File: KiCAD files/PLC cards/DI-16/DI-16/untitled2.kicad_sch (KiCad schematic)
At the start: 28 parts

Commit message: pcbs
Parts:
- removed D? (x8): (no value), symbol Device:LED_Small
- removed J? (x2): (no value), symbol Connector_Generic:Conn_02x06_Odd_Even
- removed R? (x8): (no value), symbol Device:R_Small
- removed RN? (x2): (no value), symbol Device:R_Network04
- removed U? (x8): (no value), symbol Isolator:4N25
- added D10, D11, D12, D13, D14, D15, D16, D9: LED_Small, symbol Device:LED_Small
- added J7, J8: Conn_02x06_Odd_Even, symbol Connector_Generic:Conn_02x06_Odd_Even
- added R10, R11, R12, R13, R14, R15, R16, R17: R_Small, symbol Device:R_Small
- added RN6, RN8: 330, Resistor_THT:R_Array_SIP5, symbol Device:R_Network04
- added RN7, RN9: 100k, Resistor_THT:R_Array_SIP5, symbol Device:R_Network04
- added U14, U15, U16, U17, U18, U19, U20, U21: 4N25, Package_DIP:DIP-6_W7.62mm, symbol Isolator:4N25
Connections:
- net +5V: now also RN6.1 (common), RN8.1 (common)
- net D08: now also D12.1 (K), U17.5
- net D09: now also D11.1 (K), U16.5
- net D10: now also D10.1 (K), U15.5
- net D11: now also D9.1 (K), U14.5
- net D12: now also D16.1 (K), U21.5
- net D13: now also D15.1 (K), U20.5
- net D14: now also D14.1 (K), U19.5
- net D15: now also D13.1 (K), U18.5
- net Earth_Protective: now also J7.10 (Pin_10), J7.3 (Pin_3), J7.4 (Pin_4), J7.9 (Pin_9), J8.10 (Pin_10), J8.3 (Pin_3), J8.4 (Pin_4), J8.9 (Pin_9)
- net GND: now also RN7.1 (common), RN9.1 (common), U14.4, U15.4, U16.4, U17.4, U18.4, U19.4, U20.4, U21.4
- new net: R16.1, U20.1
- new net: J8.6 (Pin_6), R16.2
- new net: R10.1, U14.1
- new net: J7.12 (Pin_12), R10.2
- new net: D14.2 (A), RN8.3 (R2)
- new net: R11.1, U15.1
- new net: J7.7 (Pin_7), U15.2
- new net: RN7.3 (R2), U15.6
- new net: R17.1, U21.1
- new net: J8.2 (Pin_2), R17.2
- new net: R12.1, U16.1
- new net: J7.5 (Pin_5), U16.2
- new net: RN7.4 (R3), U16.6
- new net: J7.1 (Pin_1), U17.2
- new net: J7.11 (Pin_11), U14.2
- new net: J7.2 (Pin_2), R13.2
- new net: J7.6 (Pin_6), R12.2
- new net: J7.8 (Pin_8), R11.2
- new net: D10.2 (A), RN6.3 (R2)
- new net: R14.1, U18.1
- new net: J8.12 (Pin_12), R14.2
- new net: J8.1 (Pin_1), U21.2
- new net: J8.11 (Pin_11), U18.2
- new net: J8.5 (Pin_5), U20.2
- new net: J8.7 (Pin_7), U19.2
- new net: J8.8 (Pin_8), R15.2
- new net: RN9.2 (R1), U18.6
- new net: RN9.4 (R3), U20.6
- new net: D9.2 (A), RN6.2 (R1)
- new net: D11.2 (A), RN6.4 (R3)
- new net: D12.2 (A), RN6.5 (R4)
- new net: RN7.2 (R1), U14.6
- new net: RN9.3 (R2), U19.6
- new net: RN9.5 (R4), U21.6
- new net: D15.2 (A), RN8.4 (R3)
- new net: D13.2 (A), RN8.2 (R1)
- new net: D16.2 (A), RN8.5 (R4)
- new net: R15.1, U19.1
- new net: RN7.5 (R4), U17.6
- new net: R13.1, U17.1
- no-connect marks 8 -> 0

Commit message: pcbs
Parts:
- R10, R11, R12, R13, R14, R15, R16, R17: value R_Small -> (none)
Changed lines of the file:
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@@
     (in_bom yes) (on_board yes) (fields_autoplaced)
     (property "Reference" "R16" (id 0) (at 223.52 76.2 90))
-    (property "Value" "R_Small" (id 1) (at 223.52 78.74 90))
+    (property "Value" "" (id 1) (at 223.52 78.74 90))
     (property "Footprint" "" (id 2) (at 223.52 82.55 0)
       (effects (font (size 1.27 1.27)) hide)
@@
     (in_bom yes) (on_board yes) (fields_autoplaced)
     (property "Reference" "R10" (id 0) (at 77.47 114.3 90))
-    (property "Value" "R_Small" (id 1) (at 77.47 116.84 90))
+    (property "Value" "" (id 1) (at 77.47 116.84 90))
     (property "Footprint" "" (id 2) (at 77.47 120.65 0)
       (effects (font (size 1.27 1.27)) hide)
@@
     (in_bom yes) (on_board yes) (fields_autoplaced)
     (property "Reference" "R17" (id 0) (at 226.06 57.15 90))
-    (property "Value" "R_Small" (id 1) (at 226.06 59.69 90))
+    (property "Value" "" (id 1) (at 226.06 59.69 90))
     (property "Footprint" "" (id 2) (at 226.06 63.5 0)
       (effects (font (size 1.27 1.27)) hide)
@@
     (in_bom yes) (on_board yes) (fields_autoplaced)
     (property "Reference" "R14" (id 0) (at 218.44 113.03 90))
-    (property "Value" "R_Small" (id 1) (at 218.44 115.57 90))
+    (property "Value" "" (id 1) (at 218.44 115.57 90))
     (property "Footprint" "" (id 2) (at 218.44 119.38 0)
       (effects (font (size 1.27 1.27)) hide)
@@
     (in_bom yes) (on_board yes) (fields_autoplaced)
     (property "Reference" "R12" (id 0) (at 82.55 77.47 90))
-    (property "Value" "R_Small" (id 1) (at 82.55 80.01 90))
+    (property "Value" "" (id 1) (at 82.55 80.01 90))
     (property "Footprint" "" (id 2) (at 82.55 83.82 0)
       (effects (font (size 1.27 1.27)) hide)
@@
     (in_bom yes) (on_board yes) (fields_autoplaced)
     (property "Reference" "R11" (id 0) (at 80.01 96.52 90))
-    (property "Value" "R_Small" (id 1) (at 80.01 99.06 90))
+    (property "Value" "" (id 1) (at 80.01 99.06 90))
     (property "Footprint" "" (id 2) (at 80.01 102.87 0)
       (effects (font (size 1.27 1.27)) hide)
@@
     (in_bom yes) (on_board yes) (fields_autoplaced)
     (property "Reference" "R15" (id 0) (at 220.98 95.25 90))
-    (property "Value" "R_Small" (id 1) (at 220.98 97.79 90))
+    (property "Value" "" (id 1) (at 220.98 97.79 90))
     (property "Footprint" "" (id 2) (at 220.98 101.6 0)
       (effects (font (size 1.27 1.27)) hide)
@@
     (in_bom yes) (on_board yes) (fields_autoplaced)
     (property "Reference" "R13" (id 0) (at 85.09 58.42 90))
-    (property "Value" "R_Small" (id 1) (at 85.09 60.96 90))
+    (property "Value" "" (id 1) (at 85.09 60.96 90))
     (property "Footprint" "" (id 2) (at 85.09 64.77 0)
       (effects (font (size 1.27 1.27)) hide)

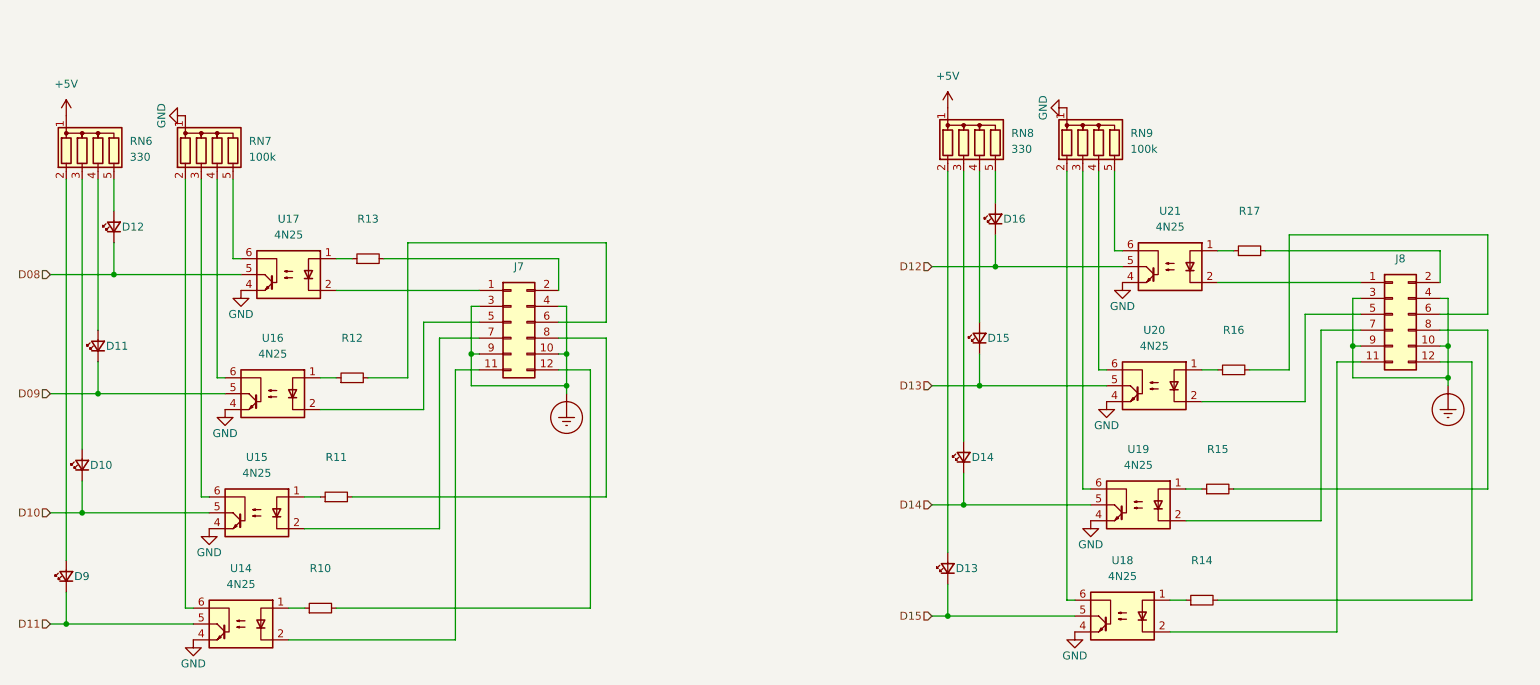
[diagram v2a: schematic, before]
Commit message: DI & DO updates
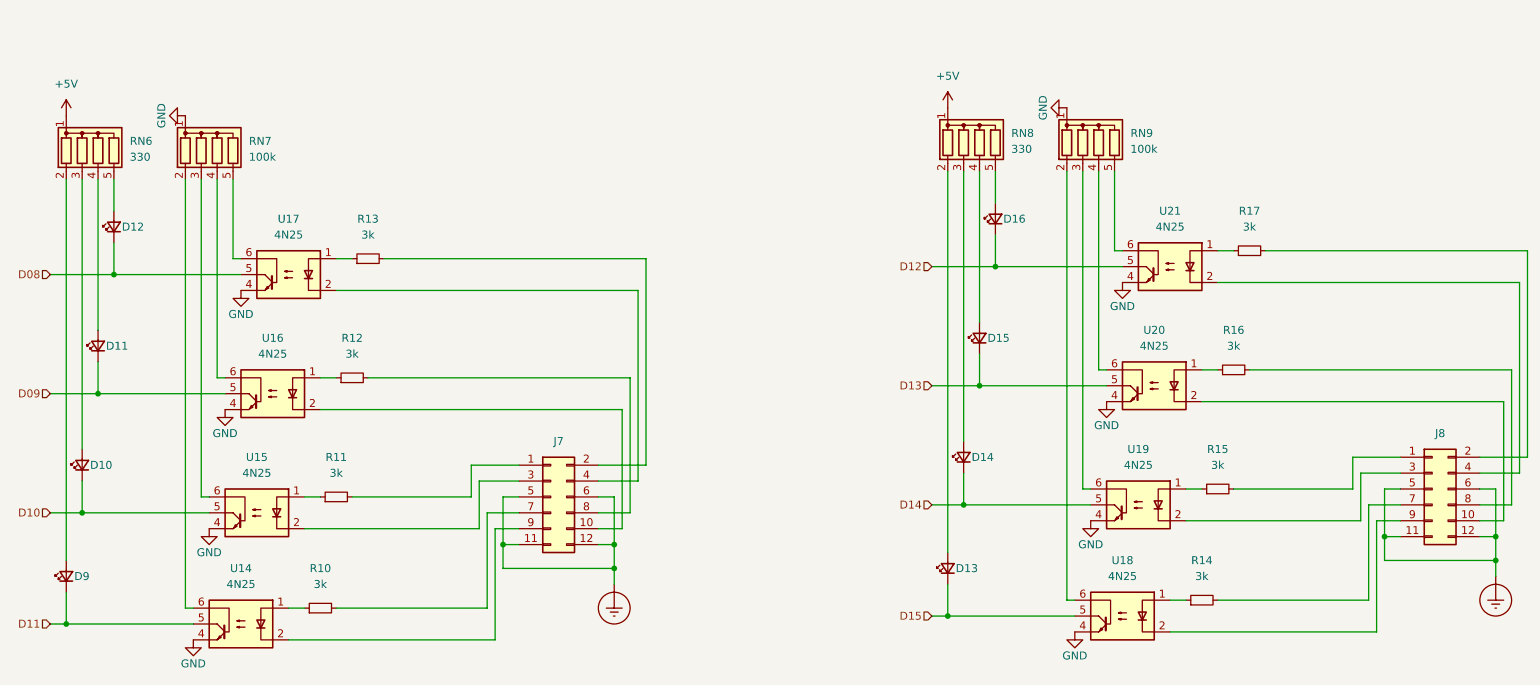
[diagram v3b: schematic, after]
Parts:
- R10, R11, R12, R13, R14, R15, R16, R17: value (none) -> 3k
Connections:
- net Earth_Protective: now also J7.11 (Pin_11), J7.12 (Pin_12), J7.5 (Pin_5), J7.6 (Pin_6), J8.11 (Pin_11), J8.12 (Pin_12), J8.5 (Pin_5), J8.6 (Pin_6); no longer J7.10 (Pin_10), J7.3 (Pin_3), J7.4 (Pin_4), J7.9 (Pin_9), J8.10 (Pin_10), J8.3 (Pin_3), J8.4 (Pin_4), J8.9 (Pin_9)
- net at R16.2: now also J8.8 (Pin_8); no longer J8.6 (Pin_6)
- net at R10.2: now also J7.7 (Pin_7); no longer J7.12 (Pin_12)
- net at U15.2: now also J7.3 (Pin_3); no longer J7.7 (Pin_7)
- net at U16.2: now also J7.10 (Pin_10); no longer J7.5 (Pin_5)
- net at J7.1 (Pin_1): now also R11.2; no longer U17.2
- net at U14.2: now also J7.9 (Pin_9); no longer J7.11 (Pin_11)
- net at R12.2: now also J7.8 (Pin_8); no longer J7.6 (Pin_6)
- net at R14.2: now also J8.7 (Pin_7); no longer J8.12 (Pin_12)
- net at J8.1 (Pin_1): now also R15.2; no longer U21.2
- net at U18.2: now also J8.9 (Pin_9); no longer J8.11 (Pin_11)
- net at U20.2: now also J8.10 (Pin_10); no longer J8.5 (Pin_5)
- net at U19.2: now also J8.3 (Pin_3); no longer J8.7 (Pin_7)
- new net: J7.4 (Pin_4), U17.2
- new net: J8.4 (Pin_4), U21.2
